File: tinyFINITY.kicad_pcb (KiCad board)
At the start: 2 copper layers, 97 parts, among them U1 AP131-33, U3 2xSPDT, U4 STM32F058C8Ux, U5 LP2985AIM5-1.8/NOPB, X2 8MHz

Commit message: some routing
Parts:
- removed C41: 2.2uF, custom:C_0402_CUSTOM
- removed C42, C43: 100nF, custom:C_0402_CUSTOM
- removed R28, R31: 1K, custom:R_0402_CUSTOM
- removed U5: LP2985AIM5-1.8/NOPB, custom:SOT-23-5
- added ANT1: 5400AT18A1000E, custom:CHIPANT_3216, F.Cu at (232.7, 124.2)
- added L6: 2.2nH HF, custom:R_0402_CUSTOM, F.Cu at (228.1, 124.6)
- added L7: 1nH HF, custom:R_0402_CUSTOM, F.Cu at (229.5, 124.1)
- added R36: 75R, custom:R_0402_CUSTOM, B.Cu at (237.6, 136.5)
- added TP10: GND, custom:TP_1.5x1.0, B.Cu at (238.0, 129.0)
- added TP9: AUDIO_IN, custom:TP_1.5x1.0, B.Cu at (238.0, 131.6)
- added U2: RTC6705, custom:QFN40_6x6_RTC, F.Cu at (227.6, 134.3)
- added X1: 8MHZ 20pF 30ppm, custom:crystal_5032, F.Cu at (236.9, 133.4)
- added Y1: LF2012-A5R5AA, custom:LPF20125, F.Cu at (225.2, 126.1)
- C10: footprint custom:C_0603_CUSTOM -> custom:C_0402_CUSTOM
- C21, C24, C34, C36, C38, C39, D1, R11, R13, R8, R9, TP1, TP2, TP6, X2: moved to B.Cu
- C35: value 10nF -> 100nF
- C37: value 1uF / 25V -> 100nF; footprint custom:C_0603_CUSTOM -> custom:C_0402_CUSTOM; moved to B.Cu
- C40: value 10nF -> 6.8pF HF
- R15: value 215R -> 8R; moved to B.Cu
- R16: value 215R -> 4R; moved to B.Cu
- R19: value 107R -> 2R; moved to B.Cu
- R20: value 107R -> 10k; moved to B.Cu
- R21: value 53.6R -> R; moved to B.Cu
- R22: value 53.6R -> 8R; moved to B.Cu
- R23: value 10k -> 10K; moved to B.Cu
- R24: value 27R -> 4R; moved to B.Cu
- R25: value 27R -> 47R; moved to B.Cu
- R27: value 1K -> 0R; moved to B.Cu
- R33: value 0R -> 2R; moved to B.Cu
- R34: value 10K -> R; moved to B.Cu
- R35: value 47R -> 75R; moved to B.Cu
- TP3, TP4, TP5: footprint custom:smd_1x1_round -> custom:TP_smd_0.5x0.3; moved to B.Cu
- U3: value 2xSPDT -> ts3a44159; footprint custom:UQFN10 -> custom:UQFN16; moved to B.Cu
- U4: value STM32F058C8Ux -> STM32F301K8Ux; footprint custom:UFQFPN48 -> custom:UFQFPN32; moved to B.Cu
- moved U3 265.1 mm to (235.9, 136.5), turned to 270 degrees
- moved U4 250.8 mm to (227.9, 137.1)
- moved TP4 246.8 mm to (231.2, 138.5), turned to 180 degrees
- moved TP6 244.5 mm to (238.0, 130.3)
- moved C25 243.3 mm to (234.2, 136.6), turned to 270 degrees
- moved TP5 243.1 mm to (226.8, 145.9)
- moved C17 242.5 mm to (232.5, 138.0), turned to 180 degrees
- moved C10 241.7 mm to (229.4, 141.0), turned to 90 degrees
- moved TP3 241.0 mm to (224.8, 137.4), turned to 270 degrees
- moved C27 240.4 mm to (234.9, 138.8), turned to 180 degrees
- moved C29 239.7 mm to (236.8, 137.1), turned to 180 degrees
- moved C26 239.2 mm to (235.5, 137.1), turned to 180 degrees
- moved C16 239.0 mm to (232.1, 135.7), turned to 180 degrees
- moved C18 238.4 mm to (238.2, 137.1), turned to 180 degrees
- moved L4 238.0 mm to (235.8, 137.9), turned to 180 degrees
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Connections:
- C16 pad 2: (no net) -> Net-(C16-Pad2)
- C18 pad 1: (no net) -> Net-(C18-Pad1)
- C19 pad 1: (no net) -> Net-(C19-Pad1)
- C20 pad 1: (no net) -> Net-(C20-Pad1)
- C25 pad 2: VIDEO -> VIDEO_OUT
- C26 pad 2: VIDEO -> VIDEO_OUT
- C27 pad 2: VIDEO -> VIDEO_OUT
- C35 pad 1: GND -> 3V3
- C35 pad 2: 3V3 -> GND
- C36 pad 2: Net-(C36-Pad2) -> 3V3
- C37 pad 1: VIN -> GND
- C37 pad 2: GND -> 3V3
- C38 pad 2: Net-(C36-Pad2) -> 3V3
- C39 pad 2: Net-(C36-Pad2) -> 3V3
- C40 pad 2: GND -> Net-(C40-Pad2)
- C5 pad 2: (no net) -> Net-(C5-Pad2)
- L4 pad 2: VIDEO -> VIDEO_OUT
- R10 pad 2: (no net) -> Net-(R10-Pad2)
- R15 pad 1: V_WHITE -> V_WHITE_0
- R15 pad 2: Net-(R15-Pad2) -> V_WHITE
- R16 pad 1: V_BLACK -> V_WHITE_1
- R16 pad 2: Net-(R16-Pad2) -> V_WHITE
- R19 pad 1: V_WHITE -> V_WHITE_2
- R19 pad 2: Net-(R19-Pad2) -> V_WHITE
- R20 pad 1: V_BLACK -> Net-(R20-Pad1)
- R20 pad 2: Net-(R20-Pad2) -> GND
- R21 pad 1: V_WHITE -> V_WHITE_3
- R21 pad 2: Net-(R21-Pad2) -> V_WHITE
- R22 pad 2: Net-(R22-Pad2) -> V_BLACK_0
- R23 pad 2: GND -> VIDEO_IN
- R24 pad 1: V_WHITE -> V_BLACK
- R24 pad 2: Net-(R24-Pad2) -> V_BLACK_1
- R25 pad 1: V_BLACK -> LED
- R25 pad 2: Net-(R25-Pad2) -> Net-(D1-Pad2)
- R27 pad 1: SPI_SCK -> Net-(R27-Pad1)
- R27 pad 2: 3V3 -> Net-(R27-Pad2)
- R32 pad 1: (no net) -> Net-(R32-Pad1)
- R33 pad 1: Net-(C36-Pad2) -> V_BLACK
- R33 pad 2: 3V3 -> V_BLACK_2
- R34 pad 1: Net-(R34-Pad1) -> V_BLACK
- R34 pad 2: VIDEO -> V_BLACK_3
- R35 pad 2: Net-(D1-Pad2) -> GND
- R4 pad 2: (no net) -> Net-(R4-Pad2)
- TP5 pad 1: SWCLK -> LED
- TP6 pad 1: VIDEO -> VIDEO_IN
- U3 pad 1: VIDEO_OVERLAY_WHITE -> Net-(U3-Pad1)
- U3 pad 10: VIDEO -> 3V3
- U3 pad 2: V_WHITE -> GND
- U3 pad 3: GND -> Net-(R36-Pad1)
- U3 pad 4: V_BLACK -> Net-(U3-Pad1)
- U3 pad 5: VIDEO_OVERLAY_BLACK -> Net-(R27-Pad1)
- U3 pad 6: (no net) -> VIDEO_OVERLAY_BLACK
- U3 pad 7: Net-(U3-Pad7) -> V_BLACK
- U3 pad 8: 3V3 -> VIDEO_OUT
- U3 pad 9: Net-(U3-Pad7) -> Net-(R27-Pad2)
- U4 pad 1: 1V8 -> 3V3
- U4 pad 10: Net-(R34-Pad1) -> UART_RX
- U4 pad 11: VIDEO -> (no net)
- U4 pad 12: UART_TX -> SPI_MOSI
- U4 pad 13: UART_RX -> Net-(R23-Pad1)
- U4 pad 14: (no net) -> VIDEO_IN
- U4 pad 15: Net-(R35-Pad1) -> (no net)
- U4 pad 16: (no net) -> GND
- U4 pad 17: (no net) -> 3V3
- U4 pad 18: Net-(R24-Pad2) -> V_WHITE_0
- U4 pad 19: Net-(R21-Pad2) -> V_WHITE_1
- U4 pad 2: (no net) -> Net-(U4-Pad2)
- U4 pad 20: (no net) -> V_WHITE_2
- U4 pad 21: Net-(R20-Pad2) -> VIDEO_OVERLAY_WHITE
- U4 pad 22: Net-(R16-Pad2) -> V_WHITE_3
- U4 pad 23: GND -> SWDATA
- U4 pad 24: 1V8 -> LED
- U4 pad 26: (no net) -> V_BLACK_0
- U4 pad 27: (no net) -> V_BLACK_1
- U4 pad 29: SPI_MOSI -> V_BLACK_2
- U4 pad 3: (no net) -> Net-(U4-Pad3)
- U4 pad 30: SPI_CS -> V_BLACK_3
- U4 pad 31: SPI_SCK -> Net-(R20-Pad1)
- U4 pad 32: (no net) -> GND
- U4 pad 33: (no net) -> GND
- U4 pad 4: (no net) -> SWRESET
- U4 pad 5: Net-(U4-Pad5) -> 3V3
- U4 pad 6: Net-(U4-Pad6) -> GND
- U4 pad 7: SWRESET -> SPI_CS
- U4 pad 8: GND -> SPI_SCK
- U4 pad 9: Net-(C36-Pad2) -> UART_TX
- X2 pad 1: Net-(U4-Pad5) -> Net-(U4-Pad2)
- X2 pad 3: Net-(U4-Pad6) -> Net-(U4-Pad3)
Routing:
- net GND: track 0.00 -> 100.1 mm, vias 0 -> 17
- net 3V3: track 0.00 -> 67.0 mm, vias 0 -> 5
- net VIDEO_IN: track 0.00 -> 20.0 mm, vias 0 -> 2
- net Net-(C30-Pad1): track 0.00 -> 15.6 mm
- net AUDIO: track 0.00 -> 13.7 mm
- net VIDEO_OVERLAY_BLACK: track 0.00 -> 11.5 mm
- net V_BLACK: track 0.00 -> 9.37 mm, vias 0 -> 2
- net Net-(C18-Pad1): track 0.00 -> 9.08 mm
- net VIDEO_OVERLAY_WHITE: track 0.00 -> 8.87 mm
- net Net-(U4-Pad3): track 0.00 -> 8.54 mm
- net V_WHITE: track 0.00 -> 8.42 mm
- net Net-(C20-Pad1): track 0.00 -> 8.06 mm
- net SPI_MOSI: track 0.00 -> 6.71 mm, vias 0 -> 1
- net UART_RX: track 0.00 -> 6.58 mm
- net Net-(U4-Pad2): track 0.00 -> 6.40 mm
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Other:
- board outline added: 20 x 20 mm
- net class Default: clearance 0.2 -> 0.1524; trace_width 0.25 -> 0.1524
- rule trace_clearance: 0.2 -> 0.1524
- rule trace_min: 0.2 -> 0.1524

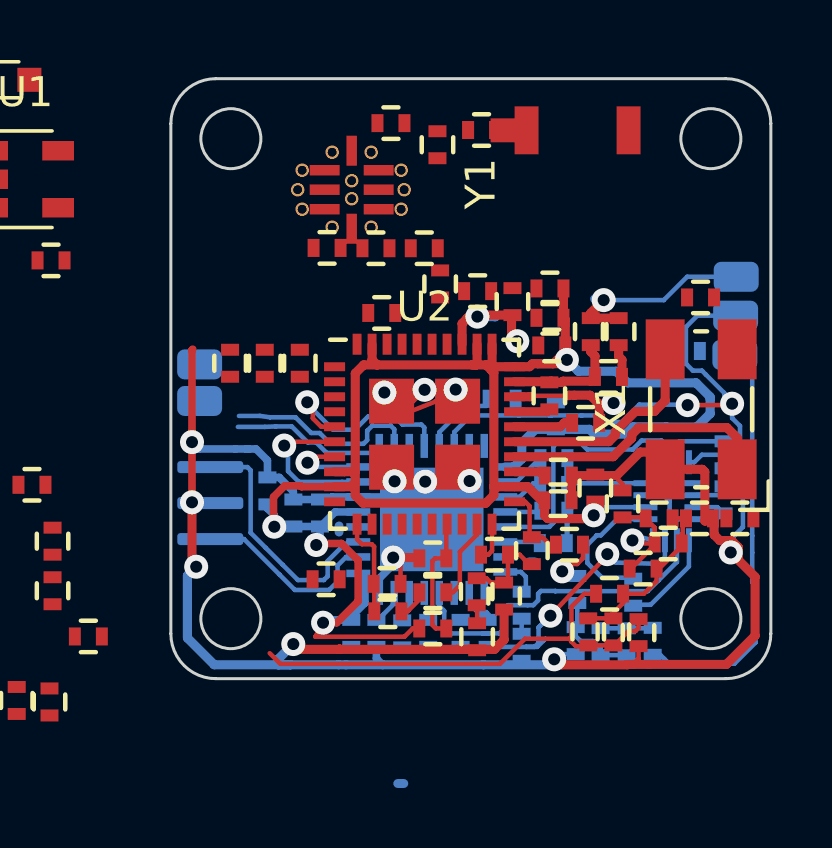
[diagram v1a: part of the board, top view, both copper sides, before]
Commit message: fixed design rules
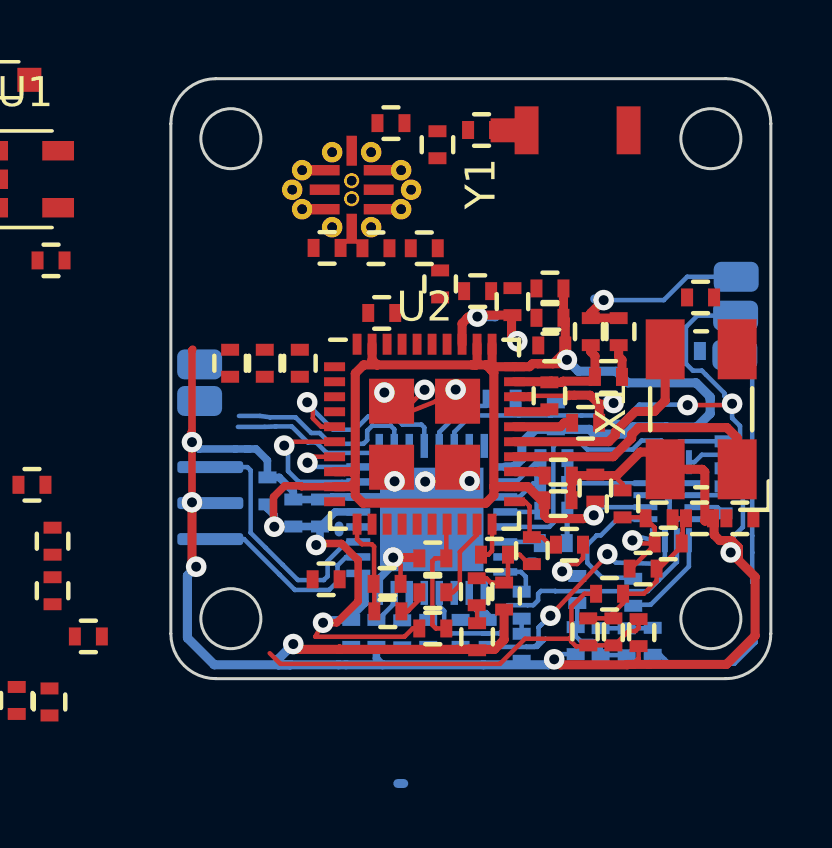
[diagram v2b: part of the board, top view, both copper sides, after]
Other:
- net class Default: via_dia 0.8 -> 0.6858; via_drill 0.4 -> 0.3302
- rule pad_to_mask_clearance: 0.2 -> 0.0762
- rule via_min_drill: 0.3 -> 0.3302
- rule via_min_size: 0.4 -> 0.6858

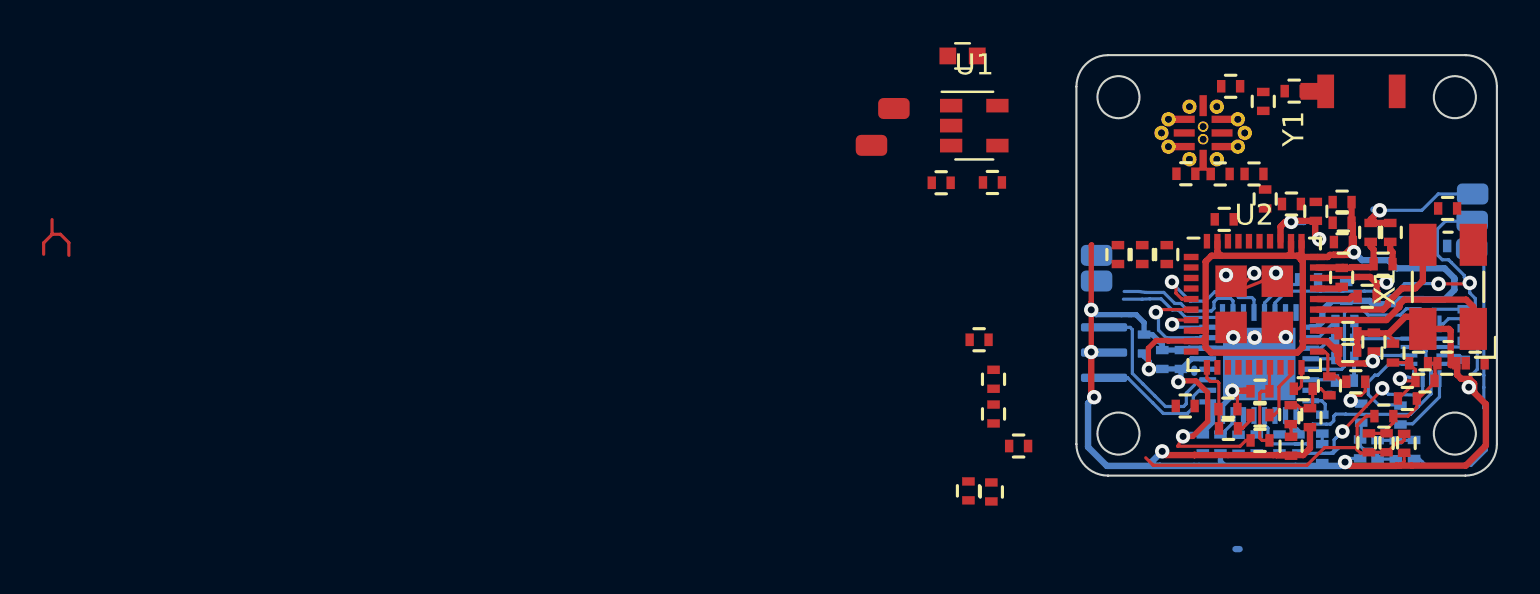
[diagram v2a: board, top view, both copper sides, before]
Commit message: some routing cleanup
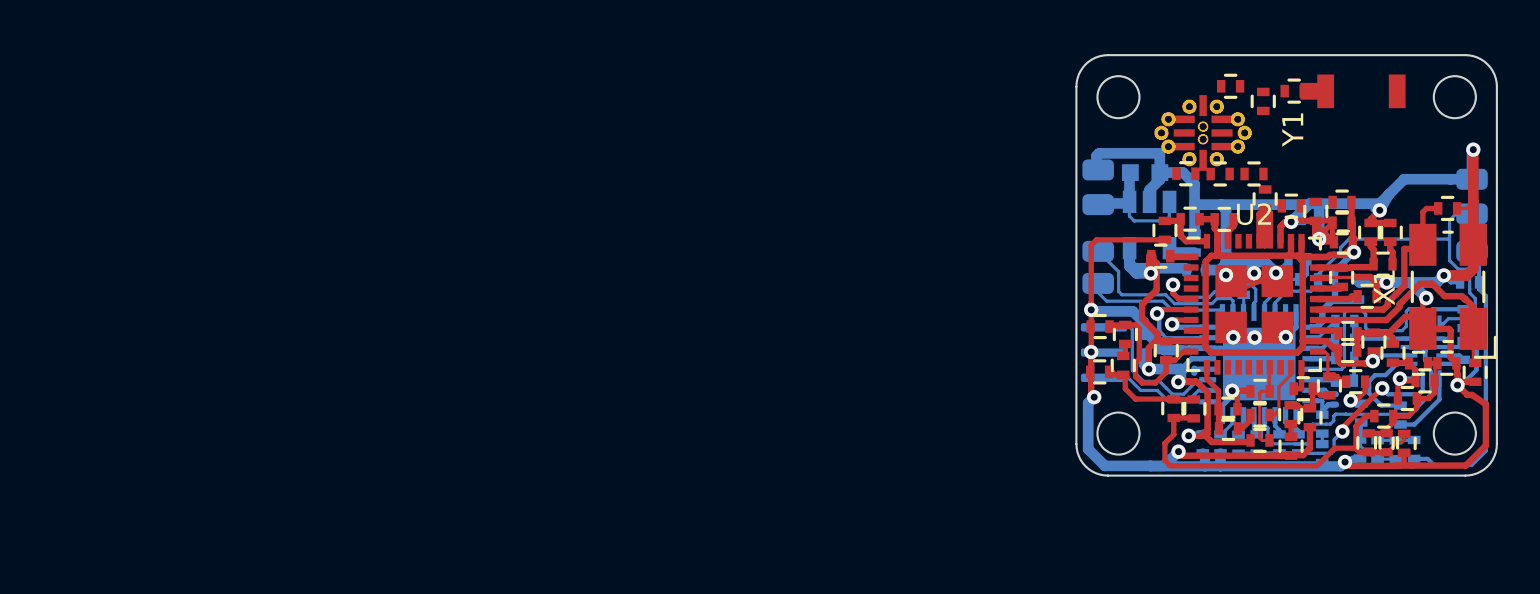
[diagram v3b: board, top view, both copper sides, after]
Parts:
- added C41: 100nF, custom:C_0402_CUSTOM, B.Cu at (227.1, 133.4)
- added C42: 10nF, custom:C_0402_CUSTOM, B.Cu at (229.7, 132.1)
- C1, C2, C28, TP7, TP8, U1: moved to B.Cu
- moved C2 12.8 mm to (224.9, 132.7), turned to 180 degrees
- moved TP7 11.1 mm to (220.2, 129.5)
- moved R17 10.5 mm to (223.8, 139.2)
- moved C32 10.4 mm to (224.8, 139.3)
- moved C28 10.3 mm to (222.5, 128.0)
- moved TP8 10.1 mm to (220.2, 127.9)
- moved C1 10.0 mm to (224.8, 131.4), turned to 270 degrees
- moved U1 9.59 mm to (222.7, 130.5), turned to 270 degrees
- moved R29 8.92 mm to (223.5, 136.5), turned to 90 degrees
- moved TP5 8.26 mm to (231.4, 139.0)
- moved R26 6.62 mm to (221.5, 135.7)
- moved C33 6.59 mm to (221.4, 137.2)
- moved R30 5.54 mm to (220.3, 135.3), turned to 0 degrees
- moved R18 5.22 mm to (220.3, 137.5), turned to 0 degrees
- moved R1 2.83 mm to (224.6, 130.2), turned to 0 degrees
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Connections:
- U4 pad 11: (no net) -> Net-(C41-Pad1)
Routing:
- net GND: track 100.1 -> 200.0 mm, vias 17 -> 20
- net 3V3: track 67.0 -> 83.4 mm, vias 5 -> 6
- net Net-(R26-Pad1): track 0.00 -> 10.1 mm
- net VIN: track 0.00 -> 6.40 mm
- net Net-(C30-Pad1): track 15.6 -> 21.5 mm
- net Net-(C32-Pad2): track 0.00 -> 5.83 mm
- net Net-(C8-Pad2): track 0.00 -> 5.10 mm
- net (no net): track 3.38 -> 0.00 mm
- net Net-(C4-Pad1): track 0.00 -> 2.93 mm
- net V_WHITE: track 8.42 -> 11.1 mm
- net V_BLACK: track 9.37 -> 11.9 mm
- net Net-(C20-Pad1): track 8.06 -> 10.5 mm
- net Net-(C18-Pad1): track 9.08 -> 11.4 mm
- net Net-(U3-Pad1): track 3.58 -> 5.90 mm
- net UART_RX: track 6.58 -> 8.78 mm
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
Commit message: routing done
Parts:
- moved C14 1.73 mm to (233.4, 129.7), turned to 180 degrees
- moved C13 0.72 mm to (231.8, 130.6)
- moved C25 0.59 mm to (234.3, 136.0)
- moved L6 0.39 mm to (228.2, 124.3)
- moved C23 0.36 mm to (233.5, 131.1)
- moved ANT1 0.35 mm to (232.7, 123.8)
- moved C22 0.35 mm to (234.4, 131.1)
- moved L7 0.34 mm to (229.6, 123.8)
- moved R6 0.30 mm to (231.8, 129.7)
- moved C9 0.29 mm to (230.6, 130.1)
- moved C26 0.24 mm to (235.2, 137.1)
- moved C4 0.18 mm to (223.2, 130.7)
- moved R3 0.18 mm to (228.1, 140.8)
- moved L3 0.17 mm to (224.4, 128.2)
- moved L2 0.17 mm to (227.7, 128.2)
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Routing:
- net GND: track 200.0 -> 274.6 mm, vias 20 -> 71
- net Net-(C40-Pad2): track 0.00 -> 3.23 mm
- net Net-(C9-Pad2): track 0.00 -> 2.94 mm
- net Net-(C15-Pad1): track 0.00 -> 2.69 mm
- net Net-(C40-Pad1): track 0.00 -> 2.15 mm
- net 3V3: track 83.4 -> 84.6 mm
- net Net-(C8-Pad2): track 5.10 -> 4.05 mm
- net Net-(ANT1-Pad1): track 0.00 -> 0.80 mm
- net VIDEO_OUT: track 5.43 -> 4.68 mm
- net Net-(C15-Pad2): track 0.00 -> 0.75 mm
- net Net-(C26-Pad1): track 8.14 -> 8.83 mm
- net UART_RX: track 8.78 -> 8.17 mm
- net Net-(C8-Pad1): track 0.00 -> 0.59 mm
- added copper zone on B.Cu, net GND
- added copper zone on F.Cu, net GND
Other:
- board text added: "+"
- board text added: "-"
- board text added: "AUDIO"
- board text added: "RX"
- board text added: "TX"
- board text added: "VIDEO"
- board text added: "fishpepper.de"
- board text added: "rev 0.1 05/17"
- board text added: "tinyFINITY"
